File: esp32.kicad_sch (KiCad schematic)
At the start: 21 parts, among them SW3 TS-1088-AR02016, SW4 TS-1088-AR02016, U7 ESP32-PICO-MINI-02-N8R2

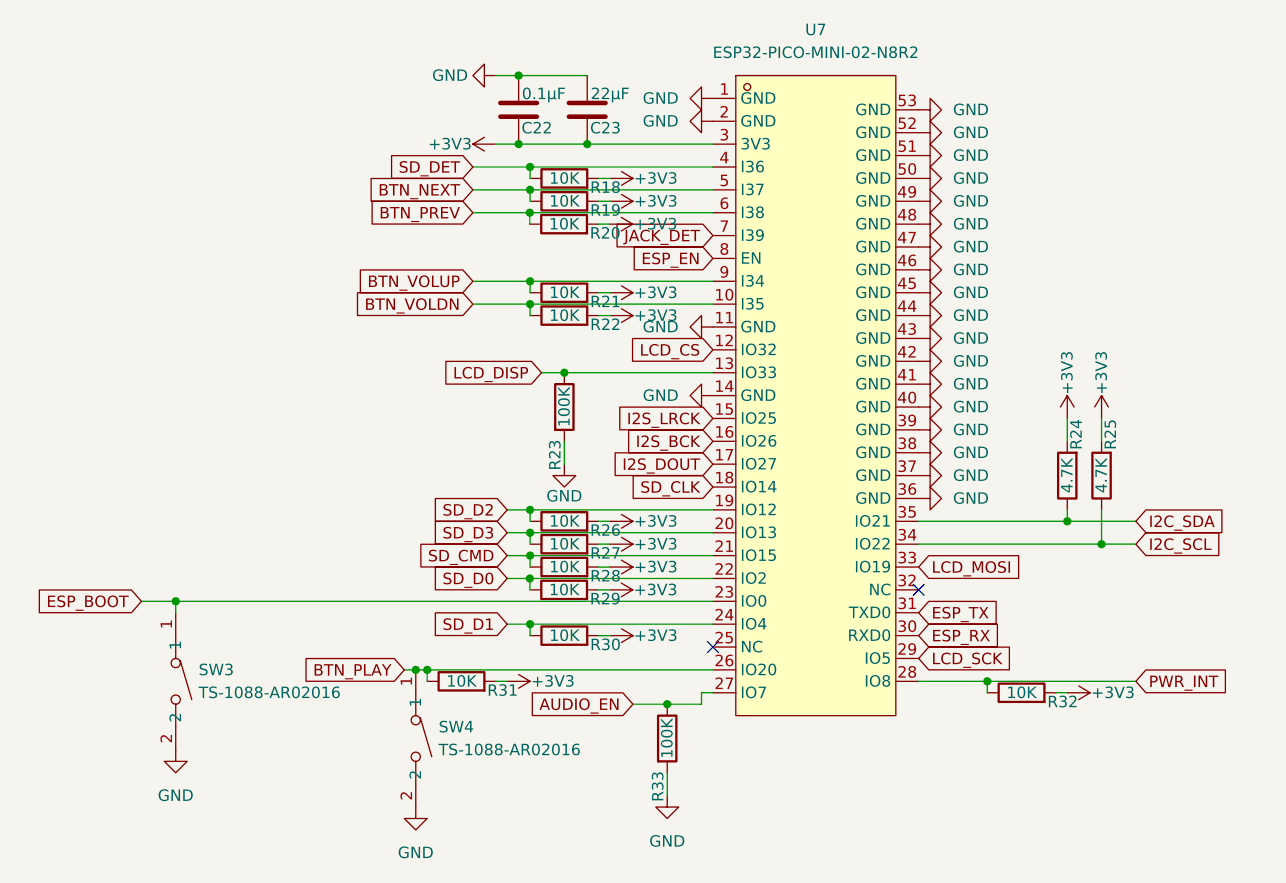
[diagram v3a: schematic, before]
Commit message: Fix ERC and document enclosure concept
- ERC clean: power flags moved onto real nets, USBLC6 pin types,
  Unspecified pins allowed in the pin conflict map, off-grid wires aligned
- mp3_player.md: enclosure section (anodized aluminium v1, titanium v2,
  printed click wheel and antenna cap, build123d workflow)
- ignore the build123d venv

Co-Authored-By: Claude Opus 5.5 <noreply@anthropic.com>
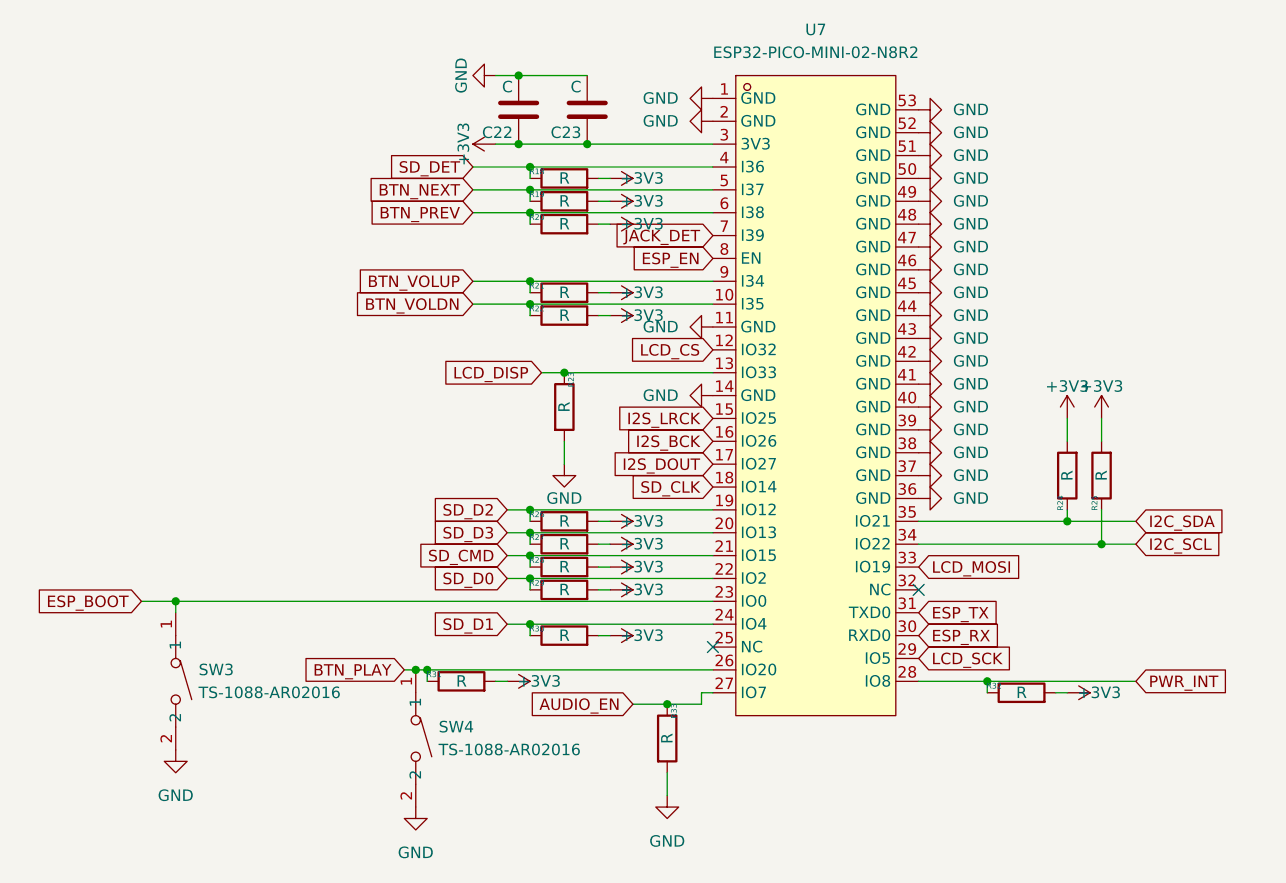
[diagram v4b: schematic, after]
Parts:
- C22: value 0.1µF -> C
- C23: value 22µF -> C
- R18, R19, R20, R21, R22, R26, R27, R28, R29, R30, R31, R32: value 10K -> R
- R23, R33: value 100K -> R
- R24, R25: value 4.7K -> R

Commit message: Schematic and parts for enclosure B
- jack PJ-342C CB (TRRS, sinking) as CN1, HP-DET on JACK_SW, MIC to GND,
  100nF on JACK_DET (detect is now active low)
- USB-C TYPE-C 16P CB0.8 073 (sinking, 0.8 mm board) as USB1
- BT1 on JST SH SM02B-SRSS-TB, click wheel on TS-1187B-B (0.75 mm),
  power on EVQP7J01P side switch
- new footprints/3D models in lib; switch and JST SH footprints renumbered
  so the existing 2-pin symbols fit
- enclosure: power key on the right side, level with the display
- docs: connections.md, code.md and BOM updated

ERC: 0 errors, 0 warnings.

Co-Authored-By: Claude Opus 5.5 <noreply@anthropic.com>
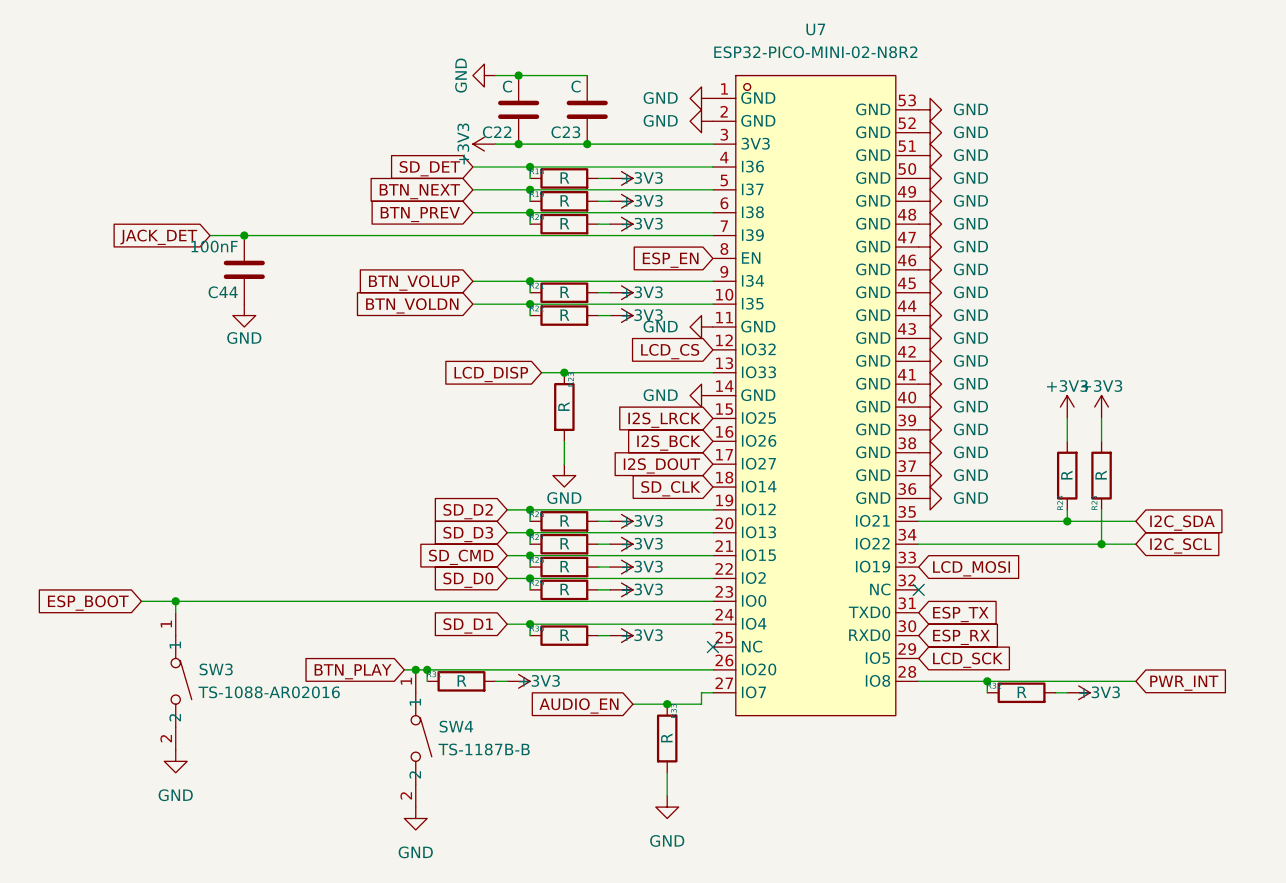
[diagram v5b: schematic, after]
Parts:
- added C44: 100nF, Capacitor_SMD:C_0402_1005Metric, symbol Device:C
- SW4: value TS-1088-AR02016 -> TS-1187B-B; footprint mp3_player:SW-SMD_L3.9-W3.0-P4.45 -> mp3_player:KEY-SMD_4P-L4.8-W4.8-P3.70-LS6.4-TL; LCSC Part C720477 -> C500066
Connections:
- net GND: now also C44.1
- net JACK_DET: now also C44.2
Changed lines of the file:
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@@
 	)
 	(junction
+		(at 77.47 77.47)
+		(diameter 0)
+		(color 0 0 0 0)
+	)
+	(junction
 		(at 109.22 107.95)
 		(diameter 0)
@@
 	(wire
 		(pts
+			(xy 73.66 77.47) (xy 77.47 77.47)
+		)
+		(stroke
+			(width 0)
+			(type default)
+		)
+	)
+	(wire
+		(pts
 			(xy 118.11 109.22) (xy 116.84 109.22)
 		)
@@
 	(wire
 		(pts
+			(xy 77.47 77.47) (xy 129.54 77.47)
+		)
+		(stroke
+			(width 0)
+			(type default)
+		)
+	)
+	(wire
+		(pts
 			(xy 109.22 120.65) (xy 129.54 120.65)
 		)
@@
 	(global_label "JACK_DET"
 		(shape input)
-		(at 129.54 77.47 180)
+		(at 73.66 77.47 180)
 		(fields_autoplaced yes)
 		(effects
@@
 		)
 		(property "Intersheetrefs" "${INTERSHEET_REFS}"
-			(at 117.6044 77.47 0)
+			(at 61.7244 77.47 0)
 			(hide yes)
 			(show_name no)
@@
 	)
 	(symbol
+		(lib_id "power:GND")
+		(at 77.47 85.09 0)
+		(unit 1)
+		(body_style 1)
+		(exclude_from_sim no)
+		(in_bom yes)
+		(on_board yes)
+		(in_pos_files yes)
+		(dnp no)
+		(property "Reference" "#PWR0153"
+			(at 77.47 91.44 0)
+			(hide yes)
+			(show_name no)
+			(do_not_autoplace no)
+			(effects
+				(font
+					(size 1.27 1.27)
+				)
+			)
+		)
+		(property "Value" "GND"
+			(at 77.47 88.9 0)
+			(show_name no)
+			(do_not_autoplace no)
+			(effects
+				(font
+					(size 1.27 1.27)
+				)
+			)
+		)
+		(property "Footprint" ""
+			(at 77.47 85.09 0)
+			(hide yes)
+			(show_name no)
+			(do_not_autoplace no)
+			(effects
+				(font
+					(size 1.27 1.27)
+				)
+			)
+		)
+		(property "Datasheet" ""
+			(at 77.47 85.09 0)
+			(hide yes)
+			(show_name no)
+			(do_not_autoplace no)
+			(effects
+				(font
+					(size 1.27 1.27)
+				)
+			)
+		)
+		(property "Description" "Power symbol creates a global label with name \"GND\" , ground"
+			(at 77.47 85.09 0)
+			(hide yes)
+			(show_name no)
+			(do_not_autoplace no)
+			(effects
+				(font
+					(size 1.27 1.27)
+				)
+			)
+		)
+		(pin "1"
+		)
+		(instances
+			(project "mp3_player"
+				(path "/e7a6a6cd-6e47-432f-a794-94ecc7288598"
+					(reference "#PWR0153")
+					(unit 1)
+				)
+			)
+		)
+	)
+	(symbol
 		(lib_id "power:+3V3")
 		(at 118.11 121.92 270)
@@
 			)
 		)
-		(property "Value" "TS-1088-AR02016"
+		(property "Value" "TS-1187B-B"
 			(at 99.06 134.6199 90)
 			(show_name no)
@@
 			)
 		)
-		(property "Footprint" "mp3_player:SW-SMD_L3.9-W3.0-P4.45"
+		(property "Footprint" "mp3_player:KEY-SMD_4P-L4.8-W4.8-P3.70-LS6.4-TL"
 			(at 88.9 133.35 0)
 			(hide yes)
@@
 			)
 		)
-		(property "LCSC Part" "C720477"
+		(property "LCSC Part" "C500066"
 			(at 78.74 133.35 0)
 			(hide yes)
@@
 					(unit 1)
 				)
+			)
+		)
+	)
+	(symbol
+		(lib_id "Device:C")
+		(at 77.47 81.28 180)
+		(unit 1)
+		(body_style 1)
+		(exclude_from_sim no)
+		(in_bom yes)
+		(on_board yes)
+		(in_pos_files yes)
+		(dnp no)
+		(property "Reference" "C44"
+			(at 76.835 83.82 0)
+			(show_name no)
+			(do_not_autoplace no)
+			(effects
+				(font
+					(size 1.27 1.27)
+				)
+				(justify left)
+			)
+		)
+		(property "Value" "100nF"
+			(at 76.835 78.74 0)
+			(show_name no)
+			(do_not_autoplace no)
+			(effects
+				(font
+					(size 1.27 1.27)
+				)
+				(justify left)
+			)
+		)
+		(property "Footprint" "Capacitor_SMD:C_0402_1005Metric"
+			(at 76.5048 77.47 0)
+			(hide yes)
+			(show_name no)
+			(do_not_autoplace no)
+			(effects
+				(font
+					(size 1.27 1.27)
+				)
+			)
+		)
+		(property "Datasheet" ""
+			(at 77.47 81.28 0)
+			(hide yes)
+			(show_name no)
+			(do_not_autoplace no)
+			(effects
+				(font
+					(size 1.27 1.27)
+				)
+			)
+		)
+		(property "Description" "Unpolarized capacitor"
+			(at 77.47 81.28 0)
+			(hide yes)
+			(show_name no)
+			(do_not_autoplace no)
+			(effects
+				(font
+					(size 1.27 1.27)
+				)
+			)
+		)
+		(property "LCSC Part" "C1525"
+			(at 76.5048 77.47 0)
+			(hide yes)
+			(show_name no)
+			(do_not_autoplace no)
+			(effects
+				(font
+					(size 1.27 1.27)
+				)
+			)
+		)
+		(pin "2"
+		)
+		(pin "1"
+		)
+		(instances
+			(project "mp3_player"
+				(path "/e7a6a6cd-6e47-432f-a794-94ecc7288598"
+					(reference "C44")
+					(unit 1)
+				)
